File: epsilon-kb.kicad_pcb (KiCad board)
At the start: 2 copper layers, 3.4 x 3 mm, 35 parts, among them J1 OLED-128x64, J2 OLED-128x32, SW1 SW_Push, SW10 SW_Push, SW11 SW_SPDT, SW2 SW_Push, SW3 SW_Push, SW4 SW_Push, SW5 SW_Push, SW6 SW_Push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

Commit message: PCB
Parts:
- added REF**: MountingHole_2.2mm_M2, MountingHole:MountingHole_2.2mm_M2, F.Cu at (132.5, 81.2)
- added REF**: MountingHole_2.2mm_M2, MountingHole:MountingHole_2.2mm_M2, F.Cu at (194.5, 126.0)
- added REF**: MountingHole_2.2mm_M2, MountingHole:MountingHole_2.2mm_M2, F.Cu at (105.5, 126.0)
- added REF**: MountingHole_2.2mm_M2, MountingHole:MountingHole_2.2mm_M2, F.Cu at (167.5, 81.2)
- added REF**: MountingHole_2.2mm_M2, MountingHole:MountingHole_2.2mm_M2, F.Cu at (239.0, 62.2)
- added REF**: MountingHole_2.2mm_M2, MountingHole:MountingHole_2.2mm_M2, F.Cu at (61.0, 62.2)
- added SW12: SW_Push, Button_Switch_THT:SW_PUSH_6mm, F.Cu at (160.8, 122.3)
- D1, D10, D2, D3, D4, D5, D6, D7, D8, D9: value SK6812MINI -> SK6812MINI-E; moved to B.Cu
- D11, D12, D13, D14, D15, D16, D17, D18, D19, D20: moved to B.Cu
- moved D14 100.0 mm to (115.8, 94.6), turned to 155 degrees
- moved D13 88.4 mm to (101.3, 83.1), turned to 155 degrees
- moved D11 85.6 mm to (61.4, 83.3), turned to 155 degrees
- moved SW4 84.7 mm to (120.0, 85.5), turned to 155 degrees
- moved D12 83.4 mm to (83.1, 79.3), turned to 155 degrees
- moved D4 83.3 mm to (122.0, 81.2), turned to 155 degrees
- moved J1 76.7 mm to (150.0, 115.7), turned to 180 degrees
- moved SW11 73.7 mm to (152.0, 127.0), turned to 180 degrees
- moved SW3 73.5 mm to (105.5, 74.0), turned to 155 degrees
- moved D3 72.0 mm to (107.5, 69.7), turned to 155 degrees
- moved SW1 70.2 mm to (65.7, 74.2), turned to 155 degrees
- moved D1 68.8 mm to (67.7, 69.9), turned to 155 degrees
- moved SW2 68.8 mm to (87.4, 70.3), turned to 155 degrees
- moved J2 67.7 mm to (127.8, 97.5)
- moved D2 67.2 mm to (89.4, 66.0), turned to 155 degrees
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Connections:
- D1 pad 1: Net-(D2-Pad3) -> +5V
- D1 pad 2: GND -> Net-(D1-Pad2)
- D1 pad 3: /LED_IN -> GND
- D1 pad 4: +5V -> /LED_IN
- D10 pad 1: /LED_OUT -> +5V
- D10 pad 2: GND -> /LED_OUT
- D10 pad 3: Net-(D10-Pad3) -> GND
- D10 pad 4: +5V -> Net-(D10-Pad4)
- D2 pad 1: Net-(D3-Pad3) -> +5V
- D2 pad 2: GND -> Net-(D2-Pad2)
- D2 pad 3: Net-(D2-Pad3) -> GND
- D2 pad 4: +5V -> Net-(D1-Pad2)
- D3 pad 1: Net-(D4-Pad3) -> +5V
- D3 pad 2: GND -> Net-(D3-Pad2)
- D3 pad 3: Net-(D3-Pad3) -> GND
- D3 pad 4: +5V -> Net-(D2-Pad2)
- D4 pad 1: Net-(D5-Pad3) -> +5V
- D4 pad 2: GND -> Net-(D4-Pad2)
- D4 pad 3: Net-(D4-Pad3) -> GND
- D4 pad 4: +5V -> Net-(D3-Pad2)
- D5 pad 1: Net-(D5-Pad1) -> +5V
- D5 pad 2: GND -> Net-(D5-Pad2)
- D5 pad 3: Net-(D5-Pad3) -> GND
- D5 pad 4: +5V -> Net-(D4-Pad2)
- D6 pad 1: Net-(D6-Pad1) -> +5V
- D6 pad 2: GND -> Net-(D6-Pad2)
- D6 pad 3: Net-(D5-Pad1) -> GND
- D6 pad 4: +5V -> Net-(D5-Pad2)
- D7 pad 1: Net-(D8-Pad3) -> +5V
- D7 pad 2: GND -> Net-(D7-Pad2)
- D7 pad 3: Net-(D6-Pad1) -> GND
- D7 pad 4: +5V -> Net-(D6-Pad2)
- D8 pad 1: Net-(D9-Pad3) -> +5V
- D8 pad 2: GND -> Net-(D8-Pad2)
- D8 pad 3: Net-(D8-Pad3) -> GND
- D8 pad 4: +5V -> Net-(D7-Pad2)
- D9 pad 1: Net-(D10-Pad3) -> +5V
- D9 pad 2: GND -> Net-(D10-Pad4)
- D9 pad 3: Net-(D9-Pad3) -> GND
- D9 pad 4: +5V -> Net-(D8-Pad2)
- U1 pad 17: unconnected-(U1-Pad17) -> /RST
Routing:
- net +5V: track 0.00 -> 318.1 mm, vias 0 -> 6
- net C2: track 0.00 -> 208.9 mm, vias 0 -> 7
- net C3: track 0.00 -> 184.1 mm, vias 0 -> 6
- net C4: track 0.00 -> 164.4 mm, vias 0 -> 8
- net C1: track 0.00 -> 160.2 mm, vias 0 -> 1
- net Net-(D8-Pad2): track 0.00 -> 144.4 mm, vias 0 -> 2
- net R1: track 0.00 -> 131.2 mm, vias 0 -> 6
- net /LED_IN: track 0.00 -> 96.9 mm, vias 0 -> 3
- net R2: track 0.00 -> 91.8 mm
- net R3: track 0.00 -> 90.2 mm, vias 0 -> 3
- net Net-(D10-Pad4): track 0.00 -> 57.5 mm, vias 0 -> 2
- net Net-(D4-Pad2): track 0.00 -> 54.3 mm
- net /RST: track 0.00 -> 46.3 mm
- net /SDA: track 0.00 -> 35.7 mm, vias 0 -> 2
- net +BATT: track 0.00 -> 35.3 mm
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- added copper zone on B.Cu, net GND
- added copper zone on F.Cu, net GND
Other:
- board size 3.4 x 3 mm -> 200.2 x 82.7 mm
- board text added: "+"
- board text added: "-"
- board text added: "3V3"
- board text added: "5V"
- board text added: "B+"
- board text added: "C1"
- board text added: "C2"
- board text added: "C3"
- board text added: "C4"
- board text added: "Epsilon by DeltaWhy version ${pcbVersion} https://github.com/DeltaWhy/epsilon-kb"
- board text added: "GND"
- board text added: "JLCJLCJLCJLC"
- board text added: "LED"
- board text added: "R1"
- board text added: "R2"
- board text added: "R3"
- board text added: "RESET"
- board text added: "RST"
- board text added: "SCL"
- board text added: "SDA"
- board text added: "x"

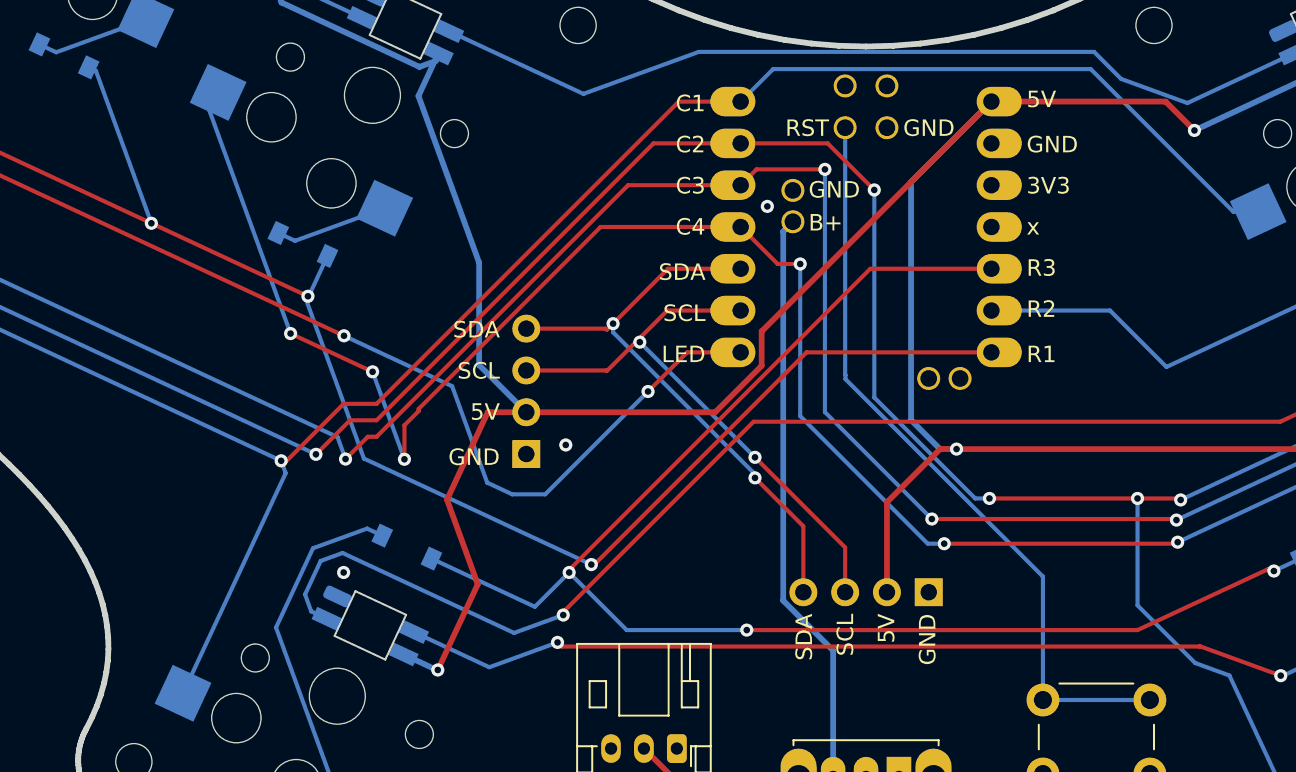
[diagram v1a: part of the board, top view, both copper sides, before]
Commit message: add Makefile and images
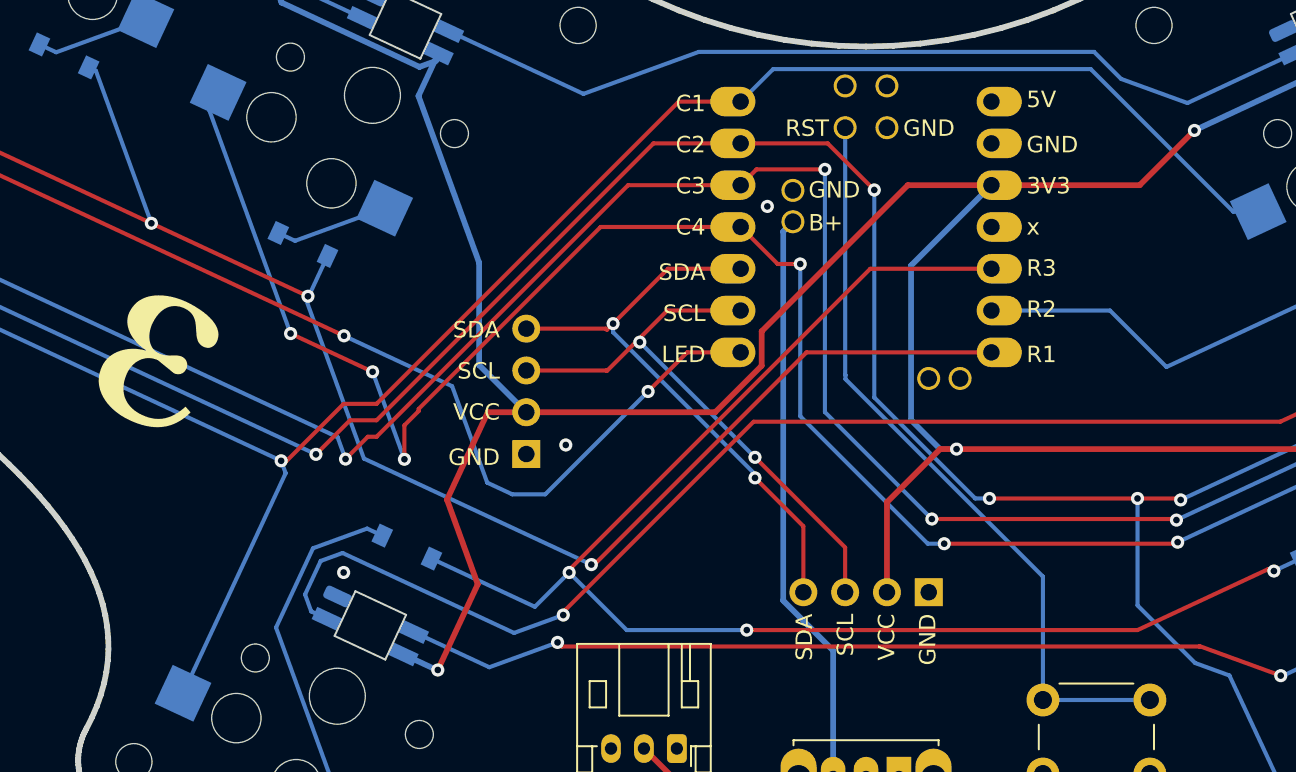
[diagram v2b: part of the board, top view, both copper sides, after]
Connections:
- D1 pad 1: +5V -> +3V3
- D10 pad 1: +5V -> +3V3
- D2 pad 1: +5V -> +3V3
- D3 pad 1: +5V -> +3V3
- D4 pad 1: +5V -> +3V3
- D5 pad 1: +5V -> +3V3
- D6 pad 1: +5V -> +3V3
- D7 pad 1: +5V -> +3V3
- D8 pad 1: +5V -> +3V3
- D9 pad 1: +5V -> +3V3
- J1 pad 2: +5V -> +3V3
- J2 pad 2: +5V -> +3V3
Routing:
- net +5V: track 318.1 -> 0.00 mm, vias 6 -> 0
- net +3V3: track 0.00 -> 311.5 mm, vias 0 -> 6
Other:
- board text added: "VCC"
